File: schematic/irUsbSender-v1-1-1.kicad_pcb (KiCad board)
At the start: 2 copper layers, 26 x 46.5 mm, 38 parts, among them J1 USB_B_Micro, J2 Conn_01x06_Male, J3 Conn_01x03_Male, J4 Conn_01x02_Male, J5 Conn_01x02_Male, J6 Conn_01x02_Male, J7 Conn_01x08_Male, Q1 IRLML6344, U1 MCP1754S-3302E_SOT23, U2 STM32F042K6Tx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

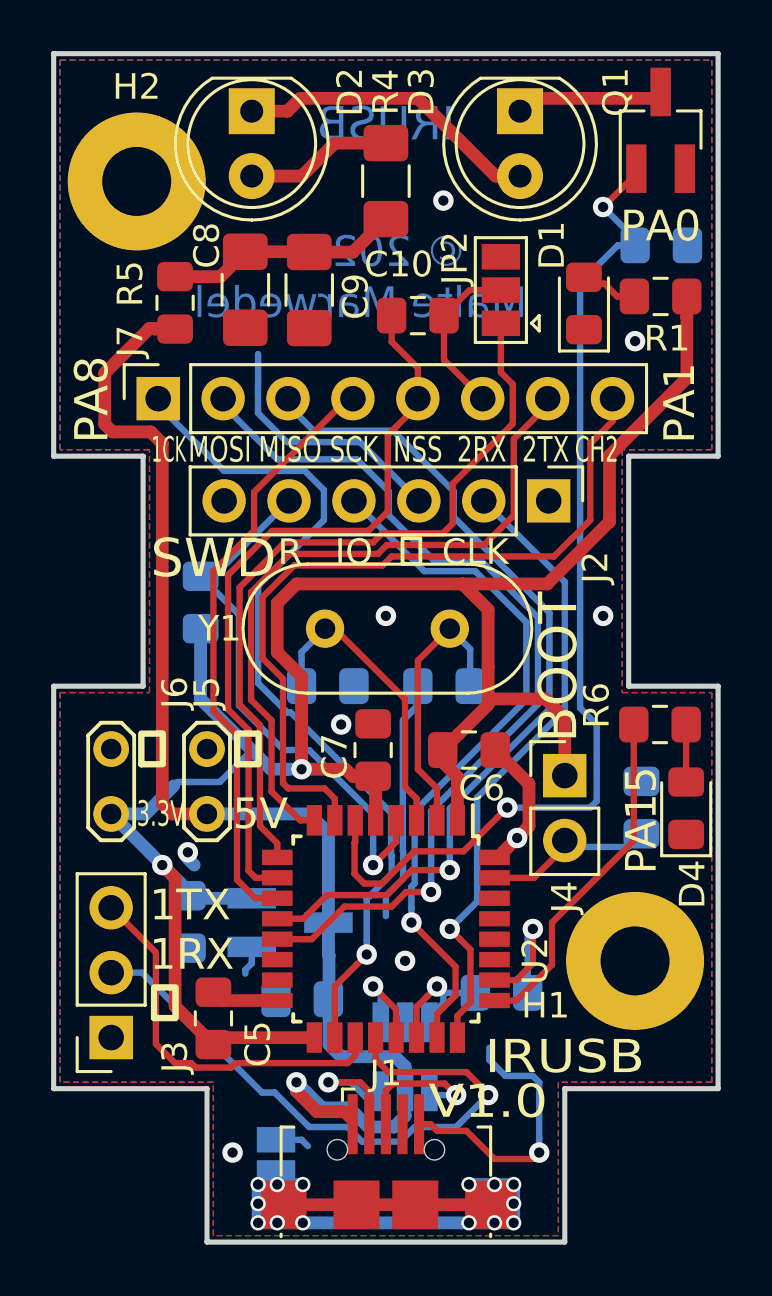
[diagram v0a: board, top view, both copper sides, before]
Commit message: Update board to version 1.1.2
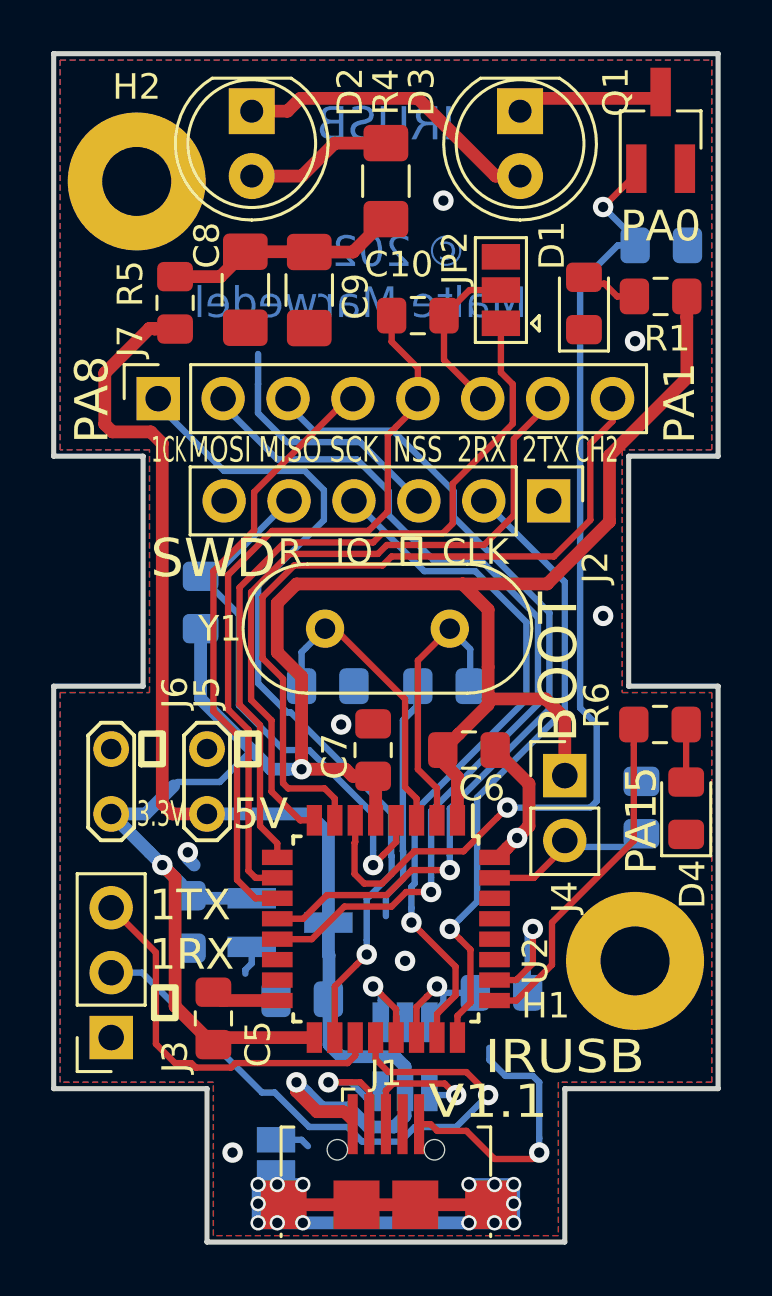
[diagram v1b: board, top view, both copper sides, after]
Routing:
- net GND: vias 10 -> 9
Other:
- board text added: "V1.1"
- board text removed: "V1.0"
